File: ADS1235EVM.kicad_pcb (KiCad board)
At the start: 2 copper layers, 50 x 25 mm, 64 parts, among them J1 Conn_01x04_Pin, J2 Conn_01x11_Pin, U1 ADS1235QWRHMRQ1, U2 LM27762, U5 UCC27524DGN

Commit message: Routing - Add of 2 ferrites bead for power
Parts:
- added REF**: L_0402_1005Metric, Inductor_SMD:L_0402_1005Metric, F.Cu at (118.4, 116.6)
- added REF**: L_0402_1005Metric, Inductor_SMD:L_0402_1005Metric, F.Cu at (129.2, 105.5)
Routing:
- net /EXT_CLK: track 14.1 -> 16.6 mm
- net GND: vias 8 -> 9
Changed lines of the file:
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@@
         (effects (font (size 1 1) (thickness 0.15)))
     )
-    (fp_text value "ADS1235QWRHMRQ1" (at 5.73 0.2511 unlocked) (layer "F.Fab")
+    (fp_text value "ADS1235QWRHMRQ1" (at 10.1 -0.3889 unlocked) (layer "F.Fab")
         (effects (font (size 1 1) (thickness 0.15)))
     )
@@
     )
   )
+  (footprint "Inductor_SMD:L_0402_1005Metric" (layer "F.Cu")
+    (at 118.42 116.565 90)
+    (descr "Inductor SMD 0402 (1005 Metric), square (rectangular) end terminal, IPC_7351 nominal, (Body size source: http://www.tortai-tech.com/upload/download/2011102023233369053.pdf), generated with kicad-footprint-generator")
+    (tags "inductor")
+    (attr smd)
+    (fp_text reference "REF**" (at 0 -1.6 90) (layer "F.SilkS") hide
+        (effects (font (size 1 1) (thickness 0.15)))
+    )
+    (fp_text value "L_0402_1005Metric" (at 0 1.17 90) (layer "F.Fab") hide
+        (effects (font (size 1 1) (thickness 0.15)))
+    )
+    (fp_text user "${REFERENCE}" (at 0 0 90) (layer "F.Fab")
+        (effects (font (size 0.25 0.25) (thickness 0.04)))
+    )
+    (fp_line (start -0.93 -0.47) (end 0.93 -0.47)
+      (stroke (width 0.05) (type solid)) (layer "F.CrtYd"))
+    (fp_line (start -0.93 0.47) (end -0.93 -0.47)
+      (stroke (width 0.05) (type solid)) (layer "F.CrtYd"))
+    (fp_line (start 0.93 -0.47) (end 0.93 0.47)
+      (stroke (width 0.05) (type solid)) (layer "F.CrtYd"))
+    (fp_line (start 0.93 0.47) (end -0.93 0.47)
+      (stroke (width 0.05) (type solid)) (layer "F.CrtYd"))
+    (fp_line (start -0.5 -0.25) (end 0.5 -0.25)
+      (stroke (width 0.1) (type solid)) (layer "F.Fab"))
+    (fp_line (start -0.5 0.25) (end -0.5 -0.25)
+      (stroke (width 0.1) (type solid)) (layer "F.Fab"))
+    (fp_line (start 0.5 -0.25) (end 0.5 0.25)
+      (stroke (width 0.1) (type solid)) (layer "F.Fab"))
+    (fp_line (start 0.5 0.25) (end -0.5 0.25)
+      (stroke (width 0.1) (type solid)) (layer "F.Fab"))
+    (pad "1" smd roundrect (at -0.485 0 90) (size 0.59 0.64) (layers "F.Cu" "F.Paste" "F.Mask") (roundrect_rratio 0.25)
+      (net 28 "/3V3"))
+    (pad "2" smd roundrect (at 0.485 0 90) (size 0.59 0.64) (layers "F.Cu" "F.Paste" "F.Mask") (roundrect_rratio 0.25)
+      (net 28 "/3V3"))
+    (model "${KICAD6_3DMODEL_DIR}/Inductor_SMD.3dshapes/L_0402_1005Metric.wrl"
+      (offset (xyz 0 0 0))
+      (scale (xyz 1 1 1))
+      (rotate (xyz 0 0 0))
+    )
+  )
   (footprint "Capacitor_SMD:C_0402_1005Metric" (layer "F.Cu")
     (at 112.01 119.07 180)
@@
     )
   )
+  (footprint "Inductor_SMD:L_0402_1005Metric" (layer "F.Cu")
+    (at 129.21 105.46)
+    (descr "Inductor SMD 0402 (1005 Metric), square (rectangular) end terminal, IPC_7351 nominal, (Body size source: http://www.tortai-tech.com/upload/download/2011102023233369053.pdf), generated with kicad-footprint-generator")
+    (tags "inductor")
+    (attr smd)
+    (fp_text reference "REF**" (at 0 -1.6) (layer "F.SilkS") hide
+        (effects (font (size 1 1) (thickness 0.15)))
+    )
+    (fp_text value "L_0402_1005Metric" (at 0 1.17) (layer "F.Fab") hide
+        (effects (font (size 1 1) (thickness 0.15)))
+    )
+    (fp_text user "${REFERENCE}" (at 0 0) (layer "F.Fab")
+        (effects (font (size 0.25 0.25) (thickness 0.04)))
+    )
+    (fp_line (start -0.93 -0.47) (end 0.93 -0.47)
+      (stroke (width 0.05) (type solid)) (layer "F.CrtYd"))
+    (fp_line (start -0.93 0.47) (end -0.93 -0.47)
+      (stroke (width 0.05) (type solid)) (layer "F.CrtYd"))
+    (fp_line (start 0.93 -0.47) (end 0.93 0.47)
+      (stroke (width 0.05) (type solid)) (layer "F.CrtYd"))
+    (fp_line (start 0.93 0.47) (end -0.93 0.47)
+      (stroke (width 0.05) (type solid)) (layer "F.CrtYd"))
+    (fp_line (start -0.5 -0.25) (end 0.5 -0.25)
+      (stroke (width 0.1) (type solid)) (layer "F.Fab"))
+    (fp_line (start -0.5 0.25) (end -0.5 -0.25)
+      (stroke (width 0.1) (type solid)) (layer "F.Fab"))
+    (fp_line (start 0.5 -0.25) (end 0.5 0.25)
+      (stroke (width 0.1) (type solid)) (layer "F.Fab"))
+    (fp_line (start 0.5 0.25) (end -0.5 0.25)
+      (stroke (width 0.1) (type solid)) (layer "F.Fab"))
+    (pad "1" smd roundrect (at -0.485 0) (size 0.59 0.64) (layers "F.Cu" "F.Paste" "F.Mask") (roundrect_rratio 0.25)
+      (net 28 "/3V3"))
+    (pad "2" smd roundrect (at 0.485 0) (size 0.59 0.64) (layers "F.Cu" "F.Paste" "F.Mask") (roundrect_rratio 0.25)
+      (net 28 "/3V3"))
+    (model "${KICAD6_3DMODEL_DIR}/Inductor_SMD.3dshapes/L_0402_1005Metric.wrl"
+      (offset (xyz 0 0 0))
+      (scale (xyz 1 1 1))
+      (rotate (xyz 0 0 0))
+    )
+  )
   (footprint "Resistor_SMD:R_0402_1005Metric" (layer "F.Cu")
     (at 123.95 118.28 -90)
@@
   (via (at 117.36 121.34) (size 0.8) (drill 0.4) (layers "F.Cu" "B.Cu") (free) (net 5))
   (via (at 144.26 119.79) (size 0.8) (drill 0.4) (layers "F.Cu" "B.Cu") (free) (net 5))
-  (via (at 125.99 102.95) (size 0.8) (drill 0.4) (layers "F.Cu" "B.Cu") (free) (net 5))
+  (via (at 126.95 107.88) (size 0.8) (drill 0.4) (layers "F.Cu" "B.Cu") (free) (net 5))
   (via (at 102.8 118.11) (size 0.8) (drill 0.4) (layers "F.Cu" "B.Cu") (free) (net 5))
   (via (at 112.05 103.36) (size 0.8) (drill 0.4) (layers "F.Cu" "B.Cu") (free) (net 5))
   (via (at 112.36 123.29) (size 0.8) (drill 0.4) (layers "F.Cu" "B.Cu") (free) (net 5))
+  (via (at 133.41 107.89) (size 0.8) (drill 0.4) (layers "F.Cu" "B.Cu") (free) (net 5))
   (via (at 104.73 105.8) (size 0.8) (drill 0.4) (layers "F.Cu" "B.Cu") (free) (net 5))
   (segment (start 145.2 118.85) (end 144.26 119.79) (width 0.5) (layer "B.Cu") (net 5))
@@
   (segment (start 119.68005 117.91) (end 121.89005 115.7) (width 0.5) (layer "B.Cu") (net 14))
   (segment (start 128.47 117.79) (end 128.47 119.11) (width 0.5) (layer "B.Cu") (net 14))
-  (segment (start 128.435 107.155) (end 128.435 105.119695) (width 0.25) (layer "F.Cu") (net 15))
+  (segment (start 129.59 108.31) (end 126.84 105.56) (width 0.25) (layer "F.Cu") (net 15))
   (segment (start 130.3089 109.6189) (end 130.3089 109.0289) (width 0.25) (layer "F.Cu") (net 15))
+  (segment (start 126.84 104.66) (end 134.96 104.66) (width 0.25) (layer "F.Cu") (net 15))
   (segment (start 130.3089 109.0289) (end 129.59 108.31) (width 0.25) (layer "F.Cu") (net 15))
-  (segment (start 129.59 108.31) (end 128.435 107.155) (width 0.25) (layer "F.Cu") (net 15))
-  (segment (start 128.894695 104.66) (end 134.96 104.66) (width 0.25) (layer "F.Cu") (net 15))
-  (segment (start 128.435 105.119695) (end 128.894695 104.66) (width 0.25) (layer "F.Cu") (net 15))
+  (segment (start 126.84 105.56) (end 126.84 104.66) (width 0.25) (layer "F.Cu") (net 15))
   (segment (start 134.96 104.66) (end 136.45 106.15) (width 0.25) (layer "F.Cu") (net 15))
   (segment (start 139.66 102.64) (end 140.85 102.64) (width 0.5) (layer "F.Cu") (net 16))
@@
   (segment (start 106.959695 114.695) (end 106.48 114.215305) (width 0.25) (layer "B.Cu") (net 27))
   (segment (start 106.48 110.22) (end 107.41 109.29) (width 0.25) (layer "B.Cu") (net 27))
-  (segment (start 118.41 116.85) (end 118.41 118.18) (width 0.5) (layer "F.Cu") (net 28))
-  (segment (start 119.55 115.51) (end 119.55 115.71) (width 0.5) (layer "F.Cu") (net 28))
-  (segment (start 130.81 105.42) (end 129.16 105.42) (width 0.5) (layer "F.Cu") (net 28))
-  (segment (start 119.55 115.71) (end 118.41 116.85) (width 0.5) (layer "F.Cu") (net 28))
+  (segment (start 127.87 105.46) (end 127.82 105.41) (width 0.25) (layer "F.Cu") (net 28))
+  (segment (start 130.81 105.42) (end 129.735 105.42) (width 0.25) (layer "F.Cu") (net 28))
+  (segment (start 118.42 117.05) (end 118.42 118.17) (width 0.25) (layer "F.Cu") (net 28))
+  (segment (start 128.725 105.46) (end 127.87 105.46) (width 0.25) (layer "F.Cu") (net 28))
+  (segment (start 127.83 105.42) (end 127.82 105.41) (width 0.5) (layer "F.Cu") (net 28))
+  (segment (start 118.42 116.08) (end 118.98 116.08) (width 0.25) (layer "F.Cu") (net 28))
+  (segment (start 129.735 105.42) (end 129.695 105.46) (width 0.25) (layer "F.Cu") (net 28))
+  (segment (start 118.42 118.17) (end 118.41 118.18) (width 0.25) (layer "F.Cu") (net 28))
+  (segment (start 118.98 116.08) (end 119.55 115.51) (width 0.25) (layer "F.Cu") (net 28))
   (via (at 119.55 115.51) (size 0.8) (drill 0.4) (layers "F.Cu" "B.Cu") (net 28))
-  (via (at 129.16 105.42) (size 0.8) (drill 0.4) (layers "F.Cu" "B.Cu") (net 28))
+  (via (at 127.82 105.41) (size 0.8) (drill 0.4) (layers "F.Cu" "B.Cu") (net 28))
   (segment (start 122.96 112.1) (end 119.55 115.51) (width 0.5) (layer "B.Cu") (net 28))
-  (segment (start 129.14 112.1) (end 129.16 105.42) (width 0.5) (layer "B.Cu") (net 28))
+  (segment (start 129.14 106.73) (end 127.82 105.41) (width 0.5) (layer "B.Cu") (net 28))
   (segment (start 147.49 117.58) (end 147.416497 117.58) (width 0.5) (layer "B.Cu") (net 28))
-  (segment (start 129.16 105.42) (end 129.14 105.42) (width 0.5) (layer "B.Cu") (net 28))
+  (segment (start 129.14 112.1) (end 129.14 106.73) (width 0.5) (layer "B.Cu") (net 28))
   (segment (start 129.14 112.1) (end 122.96 112.1) (width 0.5) (layer "B.Cu") (net 28))
   (segment (start 147.49 117.58) (end 134.62 117.58) (width 0.5) (layer "B.Cu") (net 28))
+  (segment (start 127.82 105.41) (end 127.83 105.42) (width 0.5) (layer "B.Cu") (net 28))
   (segment (start 134.62 117.58) (end 129.14 112.1) (width 0.5) (layer "B.Cu") (net 28))
   (segment (start 122.41 121.597609) (end 122.51 122.1) (width 0.25) (layer "F.Cu") (net 29))

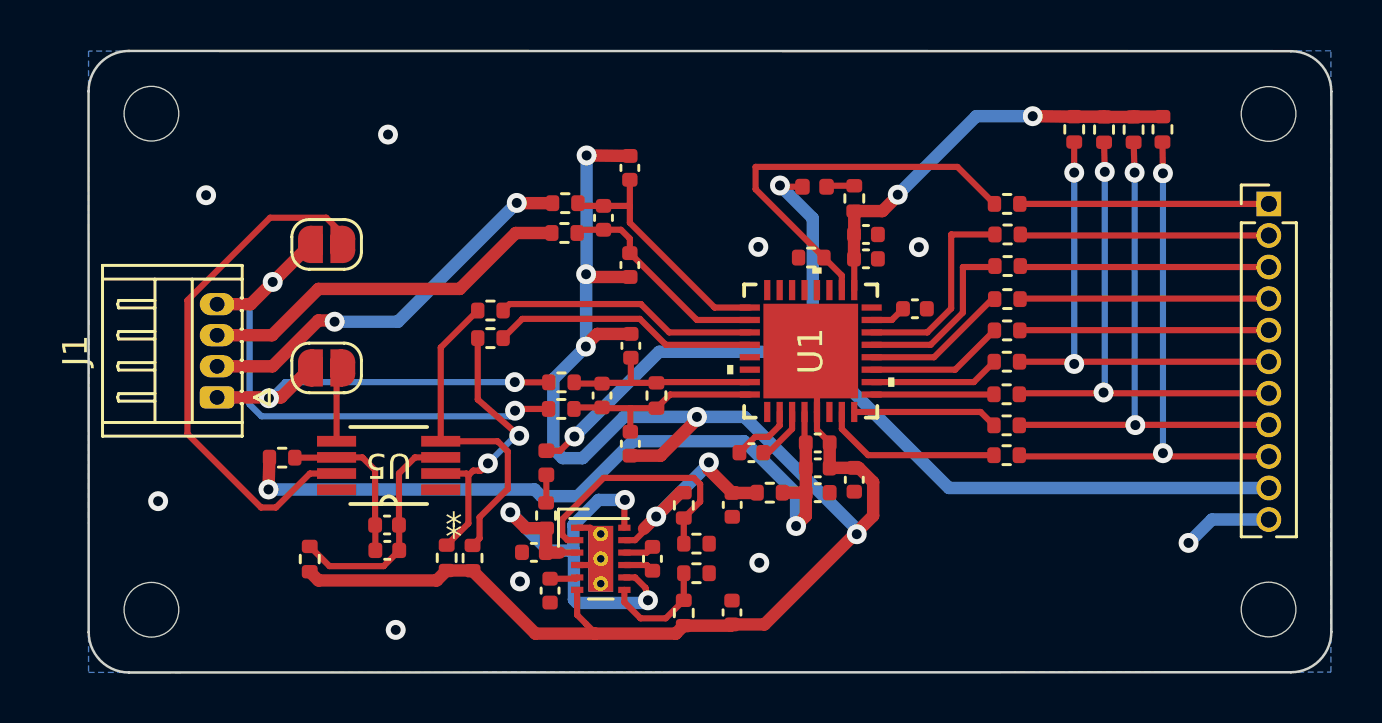
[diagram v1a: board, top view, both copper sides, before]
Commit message: Routing - Tie unused analog inputs to Avdd
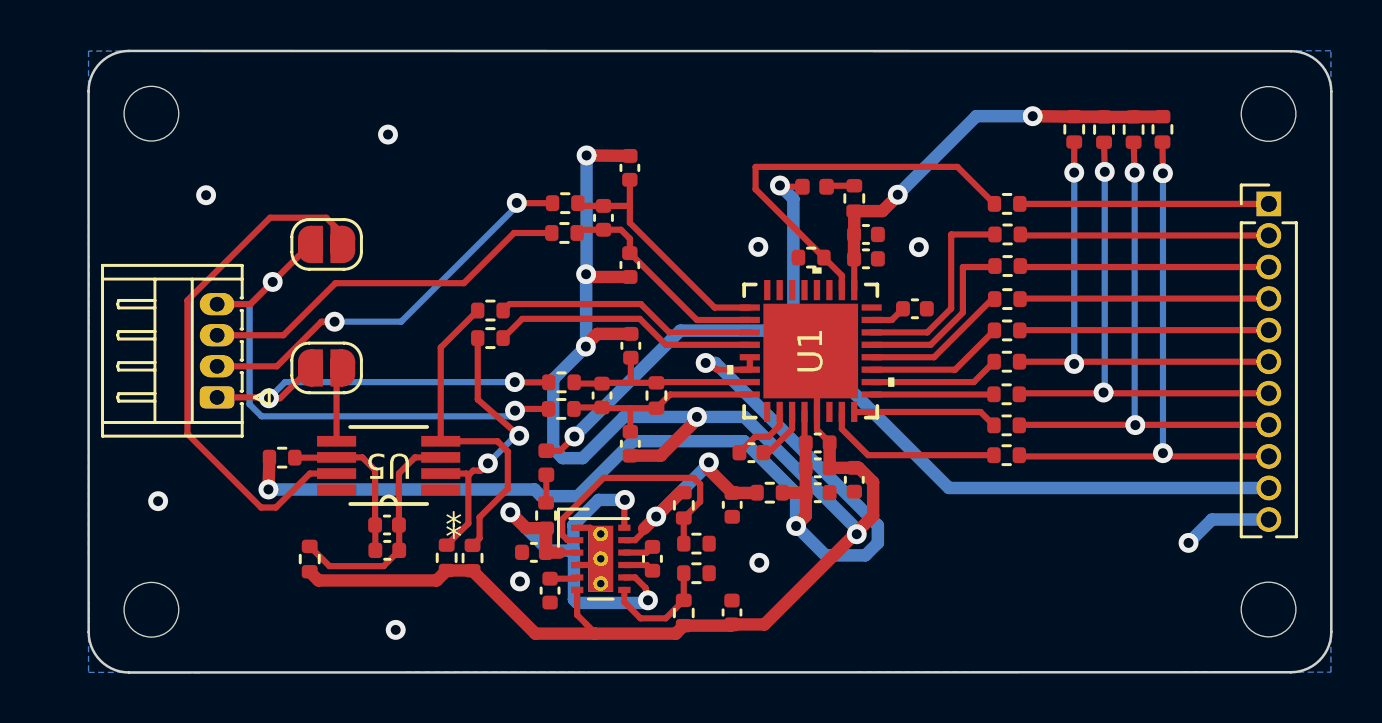
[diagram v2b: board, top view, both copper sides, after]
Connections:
- U1 pad 29: /nACX2 -> /Avdd
- U1 pad 30: /nACX1 -> /Avdd
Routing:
- net /Avdd: track 31.6 -> 48.5 mm, vias 2 -> 3
- net /3V3: track 43.5 -> 44.2 mm

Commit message: Routing - Components placement correction + DRC OK
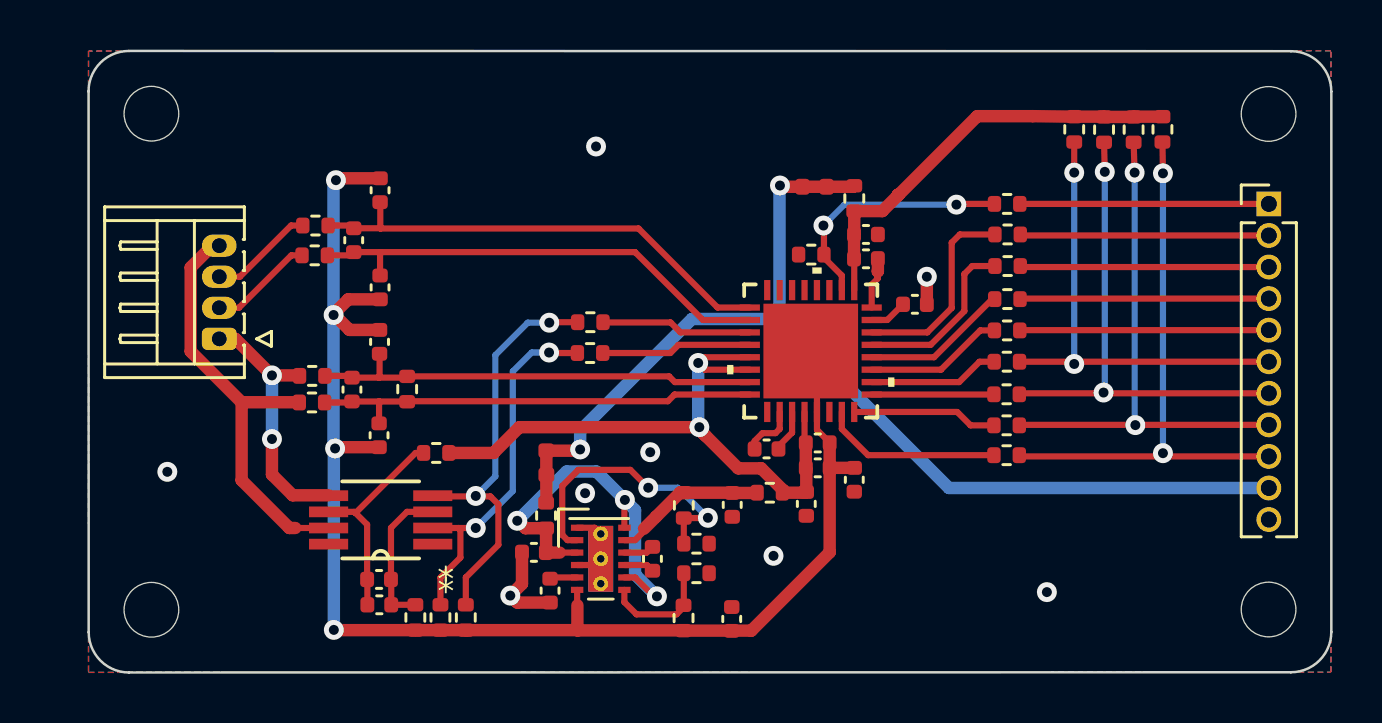
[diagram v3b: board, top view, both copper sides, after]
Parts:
- removed JP1, JP2: Jumper_2_Bridged, Jumper:SolderJumper-2_P1.3mm_Open_RoundedPad1.0x1.5mm
- moved C11 10.1 mm to (111.7, 115.5)
- moved C10 10.1 mm to (111.7, 111.7)
- moved R18 10.1 mm to (109.1, 108.2)
- moved R19 10.1 mm to (109.1, 107.0)
- moved C12 10.1 mm to (110.7, 107.6)
- moved C13 10.1 mm to (111.7, 109.5)
- moved C14 10.1 mm to (111.7, 105.6)
- moved C7 10.1 mm to (110.6, 113.6)
- moved R16 10.0 mm to (109.0, 113.1)
- moved R17 10.0 mm to (109.0, 114.1)
- moved R30 10.0 mm to (112.8, 113.6)
- moved R21 6.20 mm to (114.0, 116.2), turned to 180 degrees
- moved R20 4.86 mm to (113.2, 122.8)
- moved R33 4.05 mm to (120.2, 112.2)
- moved R34 4.05 mm to (120.2, 110.9)
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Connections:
- R18 pad 1: Net-(J1-Pin_3) -> Net-(J1-Pin_2)
- R19 pad 1: Net-(J1-Pin_2) -> Net-(J1-Pin_3)
- U5 pad 5: Net-(JP2-B) -> Net-(J1-Pin_1)
- U5 pad 7: Net-(JP1-B) -> Net-(J1-Pin_4)
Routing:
- net /Avdd: track 48.5 -> 26.7 mm, vias 3 -> 2
- net Net-(JP1-B): track 21.5 -> 0.00 mm
- net /-2.5V: track 73.5 -> 58.3 mm, vias 5 -> 4
- net Net-(J1-Pin_2): track 16.8 -> 4.20 mm, vias 2 -> 0
- net Net-(J1-Pin_3): track 15.2 -> 4.21 mm
- net Net-(U1-AIN4): track 8.85 -> 19.1 mm
- net Net-(U1-REFN0): track 8.13 -> 18.3 mm
- net Net-(U1-REFP0): track 8.29 -> 18.1 mm
- net Net-(U1-AIN5): track 10.1 -> 19.4 mm
- net /EXT_CLK: track 16.6 -> 10.3 mm, vias 0 -> 2
- net Net-(J1-Pin_4): track 22.7 -> 17.6 mm, vias 2 -> 0
- net Net-(J1-Pin_1): track 15.9 -> 11.0 mm
- net /ACX1: track 10.7 -> 6.07 mm
- net /ACX2: track 10.5 -> 6.08 mm
- net Net-(U5-INB): track 13.1 -> 17.3 mm, vias 0 -> 2
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- added copper zone on F.Cu, net GND

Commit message: PCB - Add of net names
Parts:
- moved R18 1.70 mm to (110.8, 108.0)
- moved R19 1.70 mm to (110.8, 106.9)
- moved C10 1.69 mm to (113.4, 111.4)
- moved C7 1.69 mm to (112.3, 113.3)
- moved R17 1.69 mm to (110.7, 113.8)
- moved R30 1.69 mm to (114.5, 113.3)
- moved C11 1.69 mm to (113.3, 115.1)
- moved R16 1.69 mm to (110.7, 112.8)
- moved C12 1.65 mm to (112.3, 107.5)
- moved C13 1.65 mm to (113.4, 109.4)
- moved C14 1.65 mm to (113.4, 105.5)
- moved R21 1.19 mm to (115.2, 116.4)
- moved R24 0.70 mm to (139.0, 103.3)
- moved R25 0.70 mm to (140.2, 103.3)
- moved R26 0.70 mm to (141.4, 103.3)
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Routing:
- net /-2.5V: track 58.3 -> 55.5 mm
- net Net-(J1-Pin_4): track 17.6 -> 19.5 mm
- net Net-(J1-Pin_2): track 4.20 -> 5.98 mm
- net Net-(J1-Pin_3): track 4.21 -> 5.96 mm
- net Net-(U1-REFP0): track 18.1 -> 16.4 mm
- net Net-(U1-AIN5): track 19.4 -> 17.8 mm
- net Net-(U1-REFN0): track 18.3 -> 16.8 mm
- net Net-(U1-AIN4): track 19.1 -> 17.6 mm
- net Net-(J1-Pin_1): track 11.0 -> 12.3 mm
- net Net-(U5-VDD): track 8.75 -> 9.83 mm
- net /Avdd: track 26.7 -> 25.6 mm
- net /3V3d: track 17.3 -> 16.5 mm
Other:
- board text added: "3.3V"
- board text added: "ADS1235-Q1"
- board text added: "Bipolar Supply"
- board text added: "Bridge Driver"
- board text added: "EXT_CLK"
- board text added: "GND"
- board text added: "In+"
- board text added: "In-"
- board text added: "LAAS CNRS"
- board text added: "MISO"
- board text added: "MOSI"
- board text added: "SCLK"
- board text added: "START"
- board text added: "Vex+"
- board text added: "Vex-"
- board text added: "nCS"
- board text added: "nDRDY"
- board text added: "nPWDN"
- board text added: "nRESET"
